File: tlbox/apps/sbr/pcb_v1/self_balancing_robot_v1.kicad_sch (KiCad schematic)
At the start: 0 parts

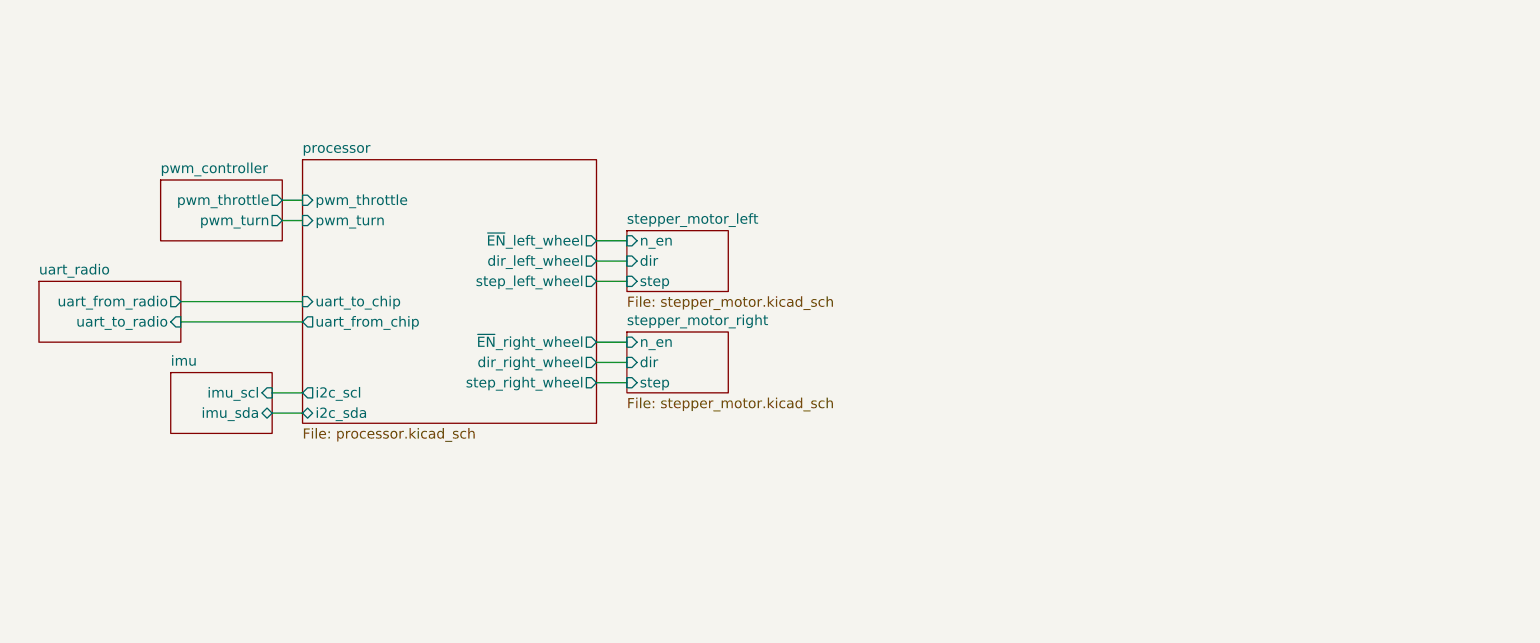
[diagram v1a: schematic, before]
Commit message: New schematic
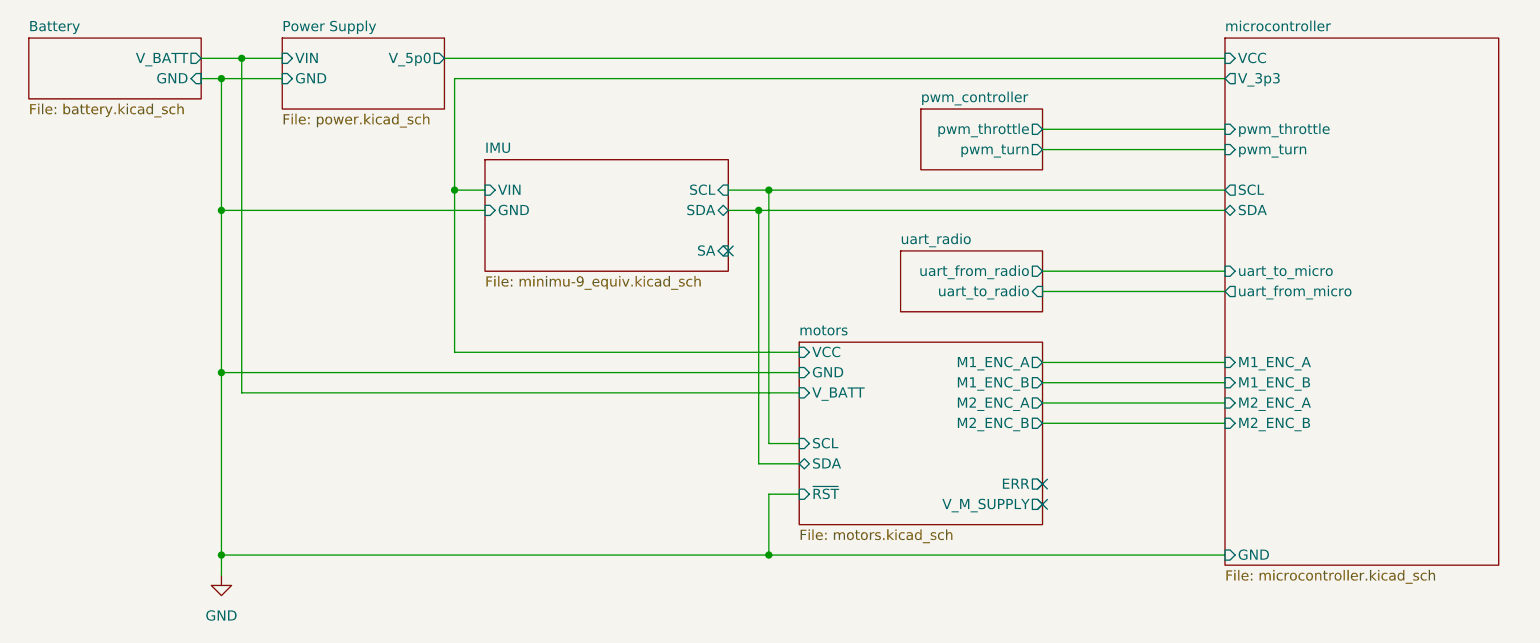
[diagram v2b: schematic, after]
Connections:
- no-connect marks 0 -> 3
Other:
- removed sheet imu
- removed sheet processor
- removed sheet stepper_motor_left
- removed sheet stepper_motor_right
- added sheet Battery (battery.kicad_sch)
- added sheet IMU (minimu-9_equiv.kicad_sch)
- added sheet Power Supply (power.kicad_sch)
- added sheet microcontroller (microcontroller.kicad_sch)
- added sheet motors (motors.kicad_sch)
